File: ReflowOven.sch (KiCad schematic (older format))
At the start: 0 parts

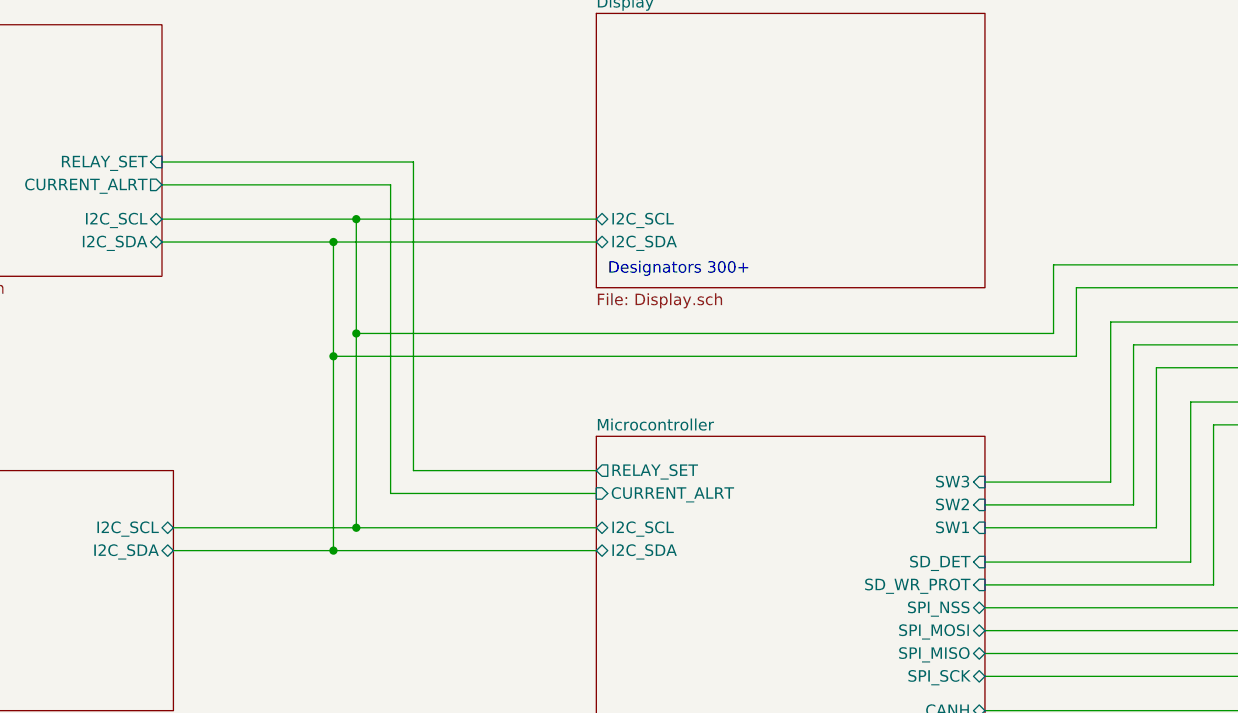
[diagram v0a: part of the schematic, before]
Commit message: Added some footprints
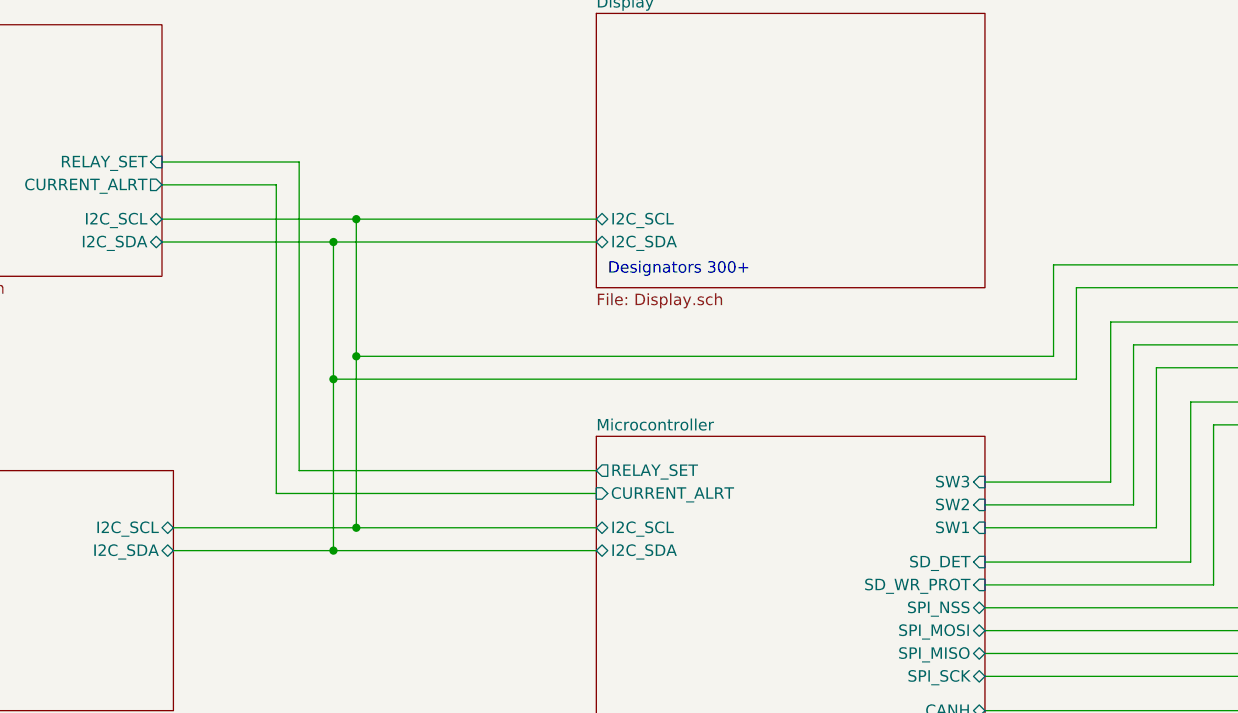
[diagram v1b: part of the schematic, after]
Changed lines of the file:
@@
 $EndSheet
 Wire Wire Line
-	4350 3750 4350 2400
+	3850 3750 3850 2400
 Wire Wire Line
-	4350 2400 3250 2400
+	3850 2400 3250 2400
 Wire Wire Line
-	4350 3750 5150 3750
+	3850 3750 5150 3750
 $Sheet
 S 1850 1800 1400 1100
@@
 $EndSheet
 Wire Wire Line
-	5150 3850 4250 3850
+	5150 3850 3750 3850
 Wire Wire Line
-	4250 3850 4250 2500
+	3750 3850 3750 2500
 Wire Wire Line
-	4250 2500 3250 2500
+	3750 2500 3250 2500
 Wire Wire Line
 	3250 2650 4100 2650
 Wire Wire Line
-	4100 2650 4100 3150
+	4100 2650 4100 3250
 Wire Wire Line
 	4100 4000 5150 4000
 Wire Wire Line
-	4000 4100 4000 3250
+	4000 4100 4000 3350
 Wire Wire Line
 	4000 2750 3250 2750
@@
 	8450 2950 7250 2950
 Wire Wire Line
-	7250 2950 7250 3250
+	7250 2950 7250 3350
 Wire Wire Line
-	7250 3250 4000 3250
-Connection ~ 4000 3250
+	7250 3350 4000 3350
+Connection ~ 4000 3350
 Wire Wire Line
-	7150 3150 7150 2850
+	7150 3250 7150 2850
 Wire Wire Line
 	7150 2850 8450 2850
 Wire Wire Line
-	4000 2750 4000 3250
+	4000 2750 4000 3350
 Wire Wire Line
-	4100 3150 7150 3150
-Connection ~ 4100 3150
+	4100 3250 7150 3250
+Connection ~ 4100 3250
 Wire Wire Line
-	4100 3150 4100 4000
+	4100 3250 4100 4000
 Wire Wire Line
 	8450 3100 7400 3100

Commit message: Began routing
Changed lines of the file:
@@
 F4 "I2C_SCL" B L 5150 4000 50
 F5 "I2C_SDA" B L 5150 4100 50
-F6 "USB_DP" B R 6850 5600 50
-F7 "USB_DM" B R 6850 5500 50
+F6 "USB_D+" B R 6850 5600 50
+F7 "USB_D-" B R 6850 5500 50
 F8 "UART_TX" O R 6850 5350 50
 F9 "UART_RX" I R 6850 5250 50
@@
 F21 "SW1" I R 6850 4000 50
 F22 "SW2" I R 6850 3900 50
+F23 "SW_BTN" I R 6850 3700 50
 $EndSheet
 $Sheet
@@
 F6 "SD_DET" O L 8450 3450 50
 F7 "SD_WR_PROT" O L 8450 3550 50
-F8 "I2C_SCL" B L 8450 2850 50
-F9 "I2C_SDA" B L 8450 2950 50
+F8 "I2C_SCL" B L 8450 2800 50
+F9 "I2C_SDA" B L 8450 2900 50
 F10 "SW1" O L 8450 3300 50
 F11 "SW2" O L 8450 3200 50
 F12 "SW3" O L 8450 3100 50
+F13 "SW_BTN" I L 8450 3000 50
 $EndSheet
 Wire Wire Line
@@
 Connection ~ 4000 2750
 Wire Wire Line
-	8450 2950 7250 2950
-Wire Wire Line
-	7250 2950 7250 3350
-Wire Wire Line
-	7250 3350 4000 3350
+	8450 2900 7200 2900
+Wire Wire Line
+	7200 2900 7200 3350
+Wire Wire Line
+	7200 3350 4000 3350
 Connection ~ 4000 3350
 Wire Wire Line
-	7150 3250 7150 2850
-Wire Wire Line
-	7150 2850 8450 2850
+	7100 3250 7100 2800
+Wire Wire Line
+	7100 2800 8450 2800
 Wire Wire Line
 	4000 2750 4000 3350
 Wire Wire Line
-	4100 3250 7150 3250
+	4100 3250 7100 3250
 Connection ~ 4100 3250
 Wire Wire Line
@@
 F0 "Communication" 50
 F1 "Communication.sch" 50
-F2 "USB_DP" B L 8450 5600 50
-F3 "USB_DM" B L 8450 5500 50
+F2 "USB_D+" B L 8450 5600 50
+F3 "USB_D-" B L 8450 5500 50
 F4 "UART_TX" I L 8450 5350 50
 F5 "UART_RX" O L 8450 5250 50
@@
 Text Notes 9400 5950 0    50   ~ 0
 Designators 700+
+Wire Wire Line
+	7300 3000 7300 3700
+Wire Wire Line
+	7300 3700 6850 3700
+Wire Wire Line
+	7300 3000 8450 3000
 $EndSCHEMATC

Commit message: Done for today with layout
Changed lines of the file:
@@
 F14 "SPI_MOSI" B R 6850 4450 50
 F15 "SPI_NSS" B R 6850 4350 50
-F16 "CANL" B R 6850 4900 50
-F17 "CANH" B R 6850 4800 50
+F16 "CAN-" B R 6850 4900 50
+F17 "CAN+" B R 6850 4800 50
 F18 "SD_WR_PROT" I R 6850 4250 50
 F19 "SD_DET" I R 6850 4150 50
@@
 F6 "UART_RTS" B L 8450 5150 50
 F7 "UART_CTS" B L 8450 5050 50
-F8 "CANH" B L 8450 4800 50
-F9 "CANL" B L 8450 4900 50
+F8 "CAN+" B L 8450 4800 50
+F9 "CAN-" B L 8450 4900 50
 $EndSheet
 Text Notes 5200 5650 0    50   ~ 0
